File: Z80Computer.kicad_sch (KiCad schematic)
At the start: 4 parts, among them U1 Z80CPU, U2 28C256, X1 CXO_DIP14

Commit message: added more components
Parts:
- added DIS1: HD44780, 16026-16X2, symbol Z80ComputerLib:HD44780
- added R1: R_Small, symbol Z80ComputerLib:R_Small
- added RV1: R_Potentiometer, symbol Device:R_Potentiometer
- added SW1: SW_Push, symbol Z80ComputerLib:SW_Push
- added U4: 74LS138, symbol Z80ComputerLib:74LS138
- added U5: 74LS00, symbol Z80ComputerLib:74LS00
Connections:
- net +5V: now also U1.16 (~{INT}), U1.17 (~{NMI}), U1.24 (~{WAIT}), U1.25 (~{BUSRQ}), U2.27 (~{WE}), DIS1.P$15, DIS1.P$2, R1.1, RV1.1, U4.16 (VCC)
- net A0: now also DIS1.P$4
- net A4: now also U4.4 (E1)
- net A5: now also U4.1 (A0)
- net A6: now also U4.2 (A1)
- net A7: now also U4.3 (A2)
- net D0: now also DIS1.P$7
- net D1: now also DIS1.P$8
- net D2: now also DIS1.P$9
- net D3: now also DIS1.P$10
- net D4: now also DIS1.P$11
- net D5: now also DIS1.P$12
- net D6: now also DIS1.P$13
- net D7: now also DIS1.P$14
- net GND: now also DIS1.P$1, DIS1.P$16, RV1.3, SW1.1, U4.8 (GND)
- net ~{RD}: now also U5.1, U5.2
- net ~{IORQ}: now reaches U1.20 (~{IORQ})
- net ~{IORQ}: now also U4.5 (E2)
- net at U1.26 (~{RESET}): now also R1.2, SW1.2
- net ~{M1}: now reaches U1.27 (~{M1})
- net ~{M1}: now also U4.6 (E3)
- new net: U4.15 (O0), U5.4, U5.5
- new net: DIS1.P$3, RV1.2
- new net: DIS1.P$5, U5.3
- new net: DIS1.P$6, U5.6
- no-connect marks 0 -> 13
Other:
- moved on the sheet: X1

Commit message: got most of the circuit done apart from key pad
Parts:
- removed U3: ~, symbol Z80ComputerLib:YouTube
- added J1: Conn_Coaxial_Power, Connector_Coaxial:SMA_Amphenol_901-143_Horizontal, symbol Connector:Conn_Coaxial_Power
- added unit 5 of U5
- added unit 4 of U5
- added unit 3 of U5
- added U6: KM62256CLP, Package_DIP:DIP-28_W15.24mm, symbol Z80ComputerLib:KM62256CLP
- added U7: 74LS00, Package_DIP:DIP-14_W7.62mm, symbol Z80ComputerLib:74LS00
- DIS1: footprint 16026-16X2 -> Downloads:16026-16X2
- R1: footprint (none) -> Resistor_THT:R_Axial_DIN0204_L3.6mm_D1.6mm_P1.90mm_Vertical
- RV1: footprint (none) -> Potentiometer_THT:Potentiometer_ACP_CA6-H2,5_Horizontal
- SW1: footprint (none) -> Button_Switch_THT:KSA_Tactile_SPST
- U1: footprint (none) -> Package_DIP:DIP-40_W25.4mm
- U2: footprint (none) -> Package_DIP:DIP-28_W15.24mm
- U4: footprint (none) -> Package_DIP:DIP-16_W7.62mm
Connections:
- net +5V: now also J1.1 (In), U5.14 (VCC), U6.28 (VCC), U7.14 (VCC)
- net A0: now also U6.10 (A0)
- net A1: now also U6.9 (A1)
- net A10: now also U6.21 (A10)
- net A11: now also U6.23 (A11)
- net A12: now also U6.2 (A12)
- net A13: now also U6.26 (A13)
- net A14: now also U6.1 (A14)
- net A15: now also U7.1, U7.4, U7.5
- net A2: now also U6.8 (A2)
- net A3: now also U6.7 (A3)
- net A4: now also U6.6 (A4)
- net A5: now also U6.5 (A5)
- net A6: now also U6.4 (A6)
- net A7: now also U6.3 (A7)
- net A8: now also U6.25 (A8)
- net A9: now also U6.24 (A9)
- net D0: now also U6.11 (Q0)
- net D1: now also U6.12 (Q1)
- net D2: now also U6.13 (Q2)
- net D3: now also U6.15 (Q3)
- net D4: now also U6.16 (Q4)
- net D5: now also U6.17 (Q5)
- net D6: now also U6.18 (Q6)
- net D7: now also U6.19 (Q7)
- net GND: now also J1.2 (Ext), U5.7 (GND), U6.14 (GND), U7.7 (GND)
- net ~{MREQ}: now also U5.10, U7.2; no longer U2.20 (~{CS})
- net ~{RD}: now also U6.22 (~{OE})
- net ~{WR}: now reaches U1.22 (~{WR})
- net ~{WR}: now also U6.27 (~{WE})
- new net: U2.20 (~{CS}), U7.3
- new net: U5.8, U6.20 (~{CS})
- new net: U5.9, U7.6
- no-connect marks 13 -> 20

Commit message: before auto route pcb
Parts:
- added C1, C2: 0.1uF, Capacitor_THT:CP_Radial_D4.0mm_P1.50mm, symbol Z80ComputerLib:C
- added D1, D2, D3, D4, D5, D6, D7, D8: 1N4148, Diode_THT:D_DO-35_SOD27_P7.62mm_Horizontal, symbol Diode:1N4148
- added D9: LED, LED_THT:LED_D5.0mm, symbol Device:LED
- added J2, J3: Conn_01x08_Pin, Connector_JST:JST_EH_B8B-EH-A_1x08_P2.50mm_Vertical, symbol Connector:Conn_01x08_Pin
- added R10: 440R, Resistor_THT:R_Axial_DIN0204_L3.6mm_D1.6mm_P1.90mm_Vertical, symbol Z80ComputerLib:R_Small
- added R2, R3, R4, R5, R6, R7, R8, R9: 10K, Resistor_THT:R_Axial_DIN0204_L3.6mm_D1.6mm_P1.90mm_Vertical, symbol Z80ComputerLib:R_Small
- added U1: 74LS244, Package_DIP:DIP-20_W7.62mm, symbol Z80ComputerLib:74LS244
- added U2: 74LS32, Package_DIP:DIP-14_W7.62mm, symbol 74xx:74LS32
- added U3: 74LS273, Package_DIP:DIP-20_W7.62mm, symbol Z80ComputerLib:74LS273
- R1: value R_Small -> 1K
- U5, U7: footprint (none) -> Package_DIP:DIP-14_W7.62mm
- renumbered U1 to IC1, U2 to IC2_EEPROM1, U6 to IC6_SRAM1
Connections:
- net +5V: now also C1.1, C2.2, D9.1 (K), U1.20 (VCC), U2.14 (VCC), U3.1 (~{Mr}), U3.20 (VCC)
- net D0: now also U1.2 (I0a), U3.3 (D0)
- net D1: now also U1.4 (I1a), U3.4 (D1)
- net D2: now also U1.6 (I2a), U3.7 (D2)
- net D3: now also U1.8 (I3a), U3.8 (D3)
- net D4: now also U1.11 (I0b), U3.13 (D4)
- net D5: now also U1.13 (I1b), U3.14 (D5)
- net D6: now also U1.15 (I2b), U3.17 (D6)
- net D7: now also U1.17 (I3b), U3.18 (D7)
- net GND: now also C1.2, C2.1, R10.2, R2.2, R3.2, R4.2, R5.2, R6.2, R7.2, R8.2, R9.2, U1.10 (GND), U2.7 (GND), U3.10 (GND)
- net ~{RD}: now also U2.2
- net ~{WR}: now also U2.4
- net ~{KEYPAD_PORT}: now reaches U4.14 (O1)
- net ~{KEYPAD_PORT}: now also U2.1, U2.5
- net ~{LCD_OUT_PORT}: now reaches U4.15 (O0), U5.4, U5.5
- new net: J2.3 (Pin_3), R7.1, U1.14 (O2a)
- new net: J2.2 (Pin_2), R8.1, U1.16 (O1a)
- new net: J2.5 (Pin_5), R5.1, U1.9 (O0b)
- new net: D1.1 (K), J3.1 (Pin_1)
- new net: D8.1 (K), J3.2 (Pin_2)
- new net: D3.1 (K), J3.3 (Pin_3)
- new net: D2.1 (K), J3.4 (Pin_4)
- new net: D4.1 (K), J3.5 (Pin_5)
- new net: D6.1 (K), J3.6 (Pin_6)
- new net: D5.1 (K), J3.7 (Pin_7)
- new net: D7.1 (K), J3.8 (Pin_8)
- new net: D7.2 (A), U3.19 (Q7)
- new net: D6.2 (A), U3.15 (Q5)
- new net: D9.2 (A), R10.1
- new net: D1.2 (A), U3.2 (Q0)
- new net: D5.2 (A), U3.16 (Q6)
- new net: J2.8 (Pin_8), R2.1, U1.3 (O3b)
- new net: D8.2 (A), U3.5 (Q1)
- new net: J2.7 (Pin_7), R4.1, U1.5 (O2b)
- new net: U2.6, U3.11 (Cp)
- new net: D4.2 (A), U3.12 (Q4)
- new net: D3.2 (A), U3.6 (Q2)
- new net: D2.2 (A), U3.9 (Q3)
- new net: J2.1 (Pin_1), R9.1, U1.18 (O0a)
- new net: J2.4 (Pin_4), R6.1, U1.12 (O3a)
- new net: U1.1 (OEa), U1.19 (OEb), U2.3
- new net: J2.6 (Pin_6), R3.1, U1.7 (O1b)
- no-connect marks 20 -> 25
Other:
- title: (none) -> Minimal Z80 Computer
- moved on the sheet: DIS1, J1, U5A, U5B, U5C, U5D, U5E, U7B, U7C, U7D, U7E

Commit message: reworked to correct z80 footprint
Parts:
- IC1: footprint Package_DIP:DIP-40_W25.4mm -> Package_DIP:DIP-40_W15.24mm
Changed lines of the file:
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@@
       (effects (font (size 1.27 1.27)) (justify left))
     )
-    (property "Footprint" "Package_DIP:DIP-40_W25.4mm" (at 109.22 86.36 0)
+    (property "Footprint" "Package_DIP:DIP-40_W15.24mm" (at 109.22 86.36 0)
       (effects (font (size 1.27 1.27)) hide)
     )

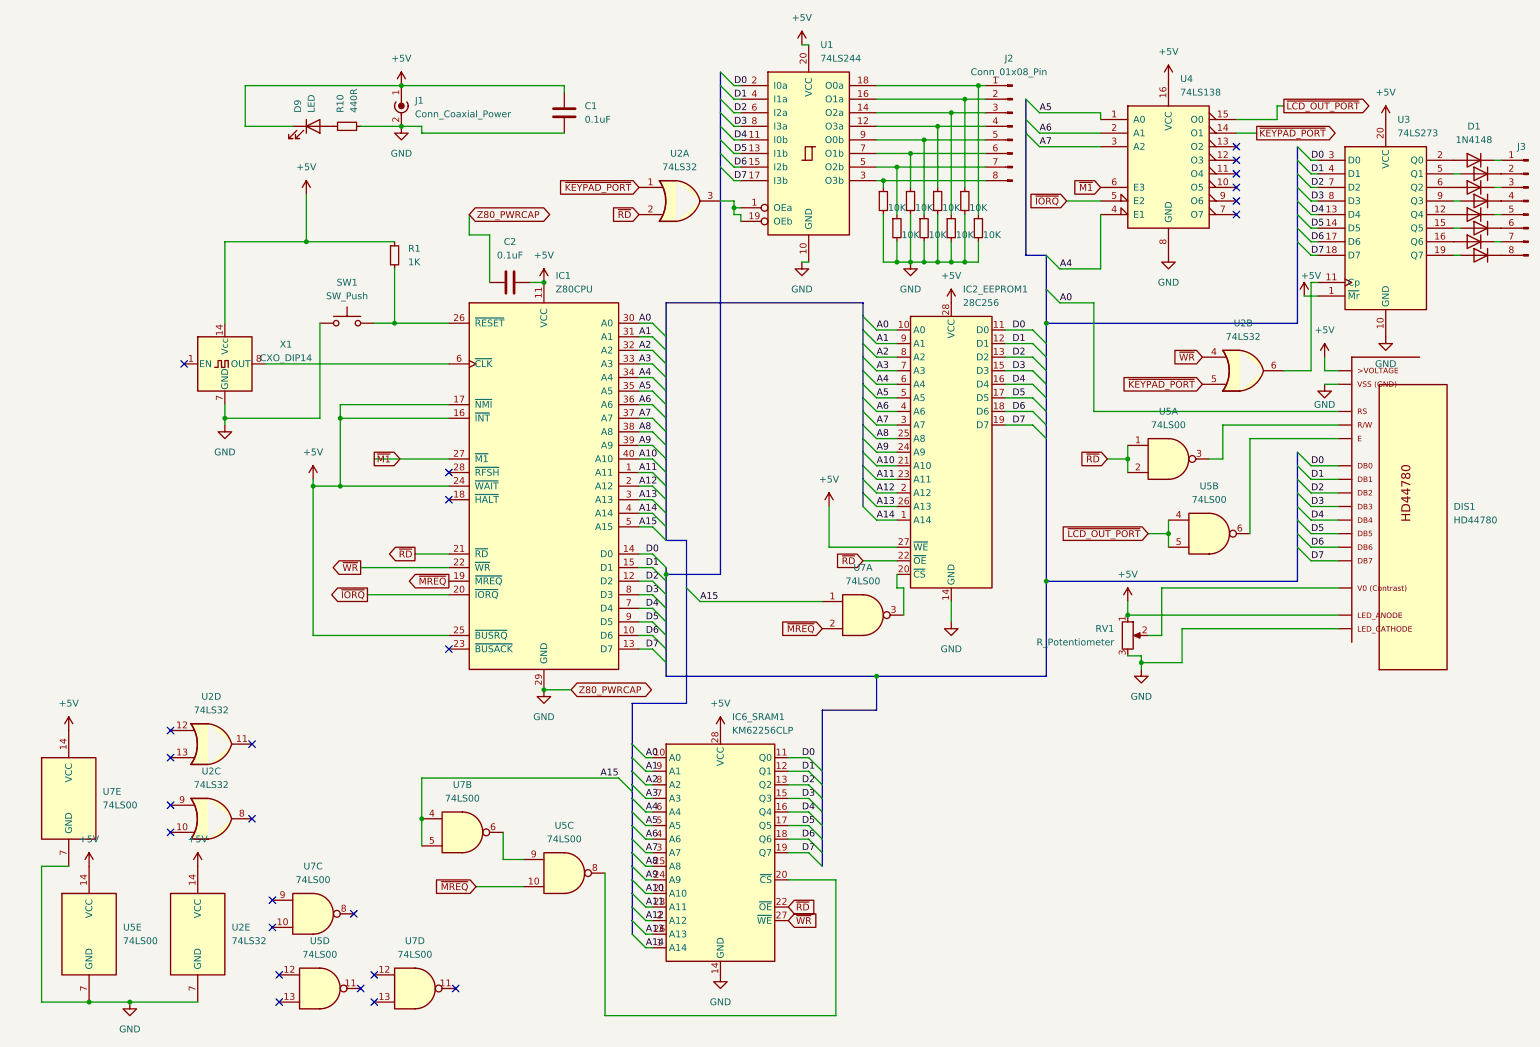
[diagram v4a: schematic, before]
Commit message: Added RC reset and fixed RAM ROM chip select
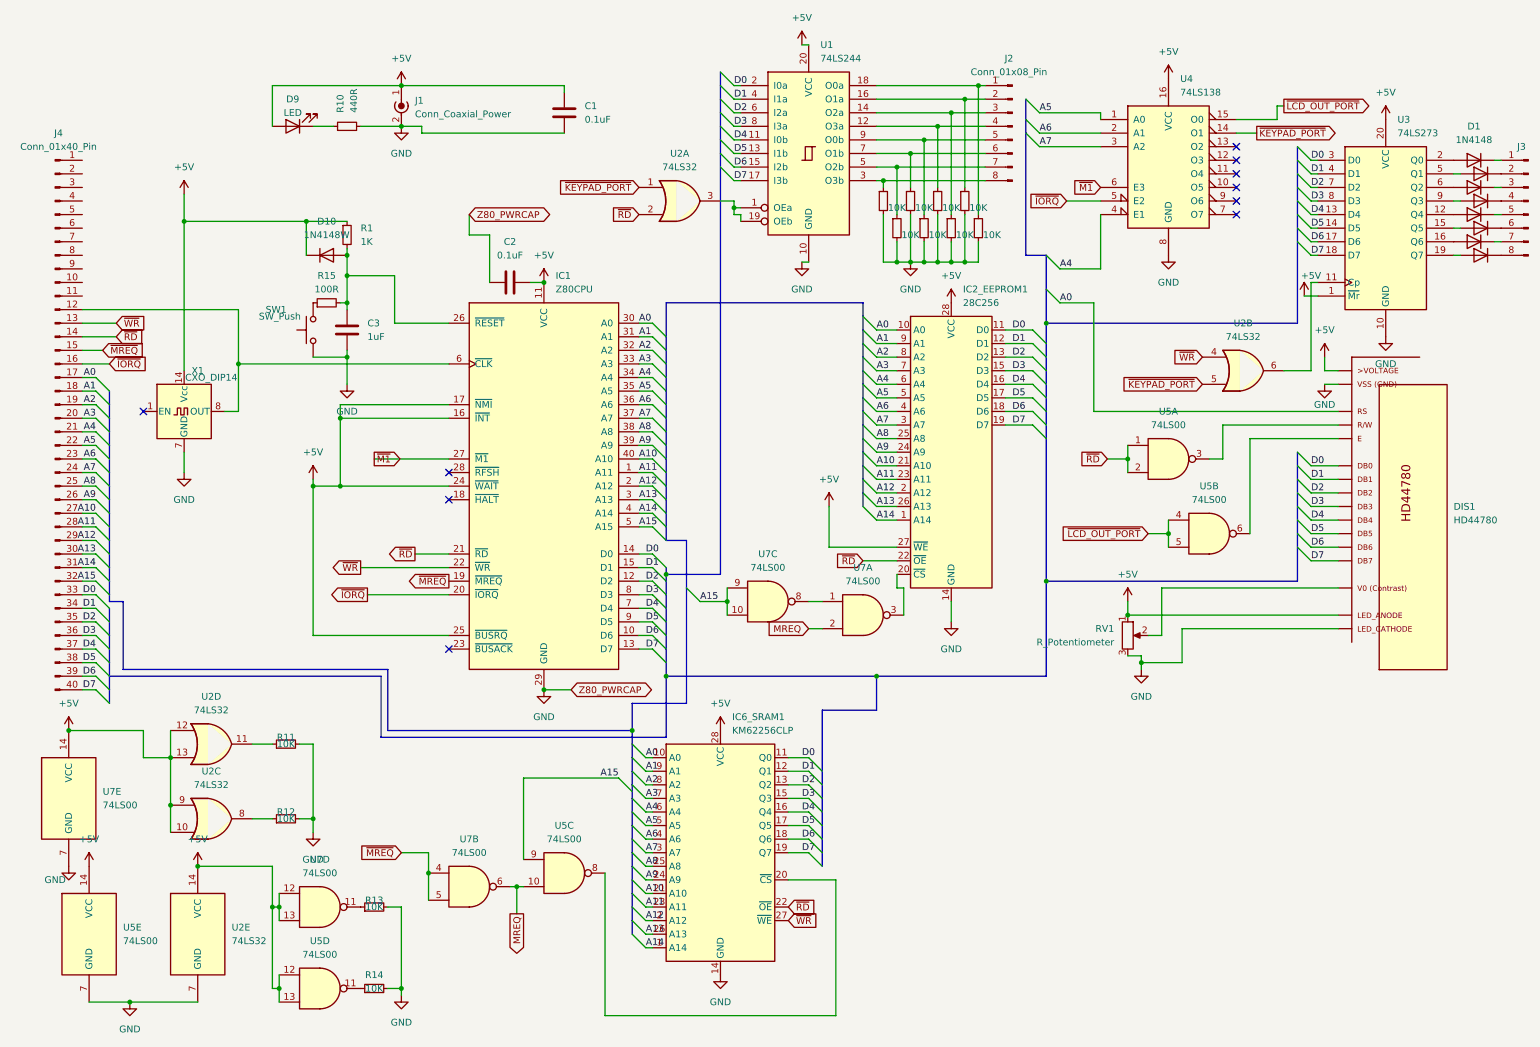
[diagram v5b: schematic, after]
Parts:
- added C3: 1uF, symbol Z80ComputerLib:C
- added D10: 1N4148W, Diode_SMD:D_SOD-123, symbol Diode:1N4148W
- added J4: Conn_01x40_Pin, symbol Connector:Conn_01x40_Pin
- added R11, R12, R13, R14: 10K, Resistor_THT:R_Axial_DIN0204_L3.6mm_D1.6mm_P1.90mm_Vertical, symbol Z80ComputerLib:R_Small
- added R15: 100R, symbol Z80ComputerLib:R_Small
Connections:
- net +5V: now also D9.2 (A), U2.10, U2.12, U2.13, U2.9, U5.12, U5.13, U7.12, U7.13, D10.1 (K); no longer D9.1 (K)
- net A0: now also J4.17 (Pin_17)
- net A1: now also J4.18 (Pin_18)
- net A10: now also J4.27 (Pin_27)
- net A11: now also J4.28 (Pin_28)
- net A12: now also J4.29 (Pin_29)
- net A13: now also J4.30 (Pin_30)
- net A14: now also J4.31 (Pin_31)
- net A15: now also U5.9, U7.10, U7.9, J4.32 (Pin_32); no longer U7.1, U7.4, U7.5
- net A2: now also J4.19 (Pin_19)
- net A3: now also J4.20 (Pin_20)
- net A4: now also J4.21 (Pin_21)
- net A5: now also J4.22 (Pin_22)
- net A6: now also J4.23 (Pin_23)
- net A7: now also J4.24 (Pin_24)
- net A8: now also J4.25 (Pin_25)
- net A9: now also J4.26 (Pin_26)
- net D0: now also J4.33 (Pin_33)
- net D1: now also J4.34 (Pin_34)
- net D2: now also J4.35 (Pin_35)
- net D3: now also J4.36 (Pin_36)
- net D4: now also J4.37 (Pin_37)
- net D5: now also J4.38 (Pin_38)
- net D6: now also J4.39 (Pin_39)
- net D7: now also J4.40 (Pin_40)
- net GND: now also C3.2, R11.2, R12.2, R13.2, R14.2
- net ~{IORQ}: now also J4.16 (Pin_16)
- net ~{MREQ}: now also U7.4, U7.5, J4.15 (Pin_15); no longer U5.10, U7.2
- net ~{RD}: now also J4.14 (Pin_14)
- net ~{WR}: now also J4.13 (Pin_13)
- net at U2.11: now also R11.1
- net at IC1.26 (~{RESET}), R1.2: now also C3.1, D10.2 (A), R15.2; no longer SW1.2
- net at R10.1: now also D9.1 (K); no longer D9.2 (A)
- net at IC1.6 (~{CLK}), X1.8 (OUT): now also J4.12 (Pin_12)
- net at U2.8: now also R12.1
- net at U7.11: now also R13.1
- net at U7.8: now also U7.1
- net at U5.11: now also R14.1
- net MREQ: now reaches U7.6
- net MREQ: now also U5.10, U7.2; no longer U5.9
- new net: R15.1, SW1.2
- no-connect marks 25 -> 10
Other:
- moved on the sheet: D9, R1, SW1, U7B, U7C, U7D, X1

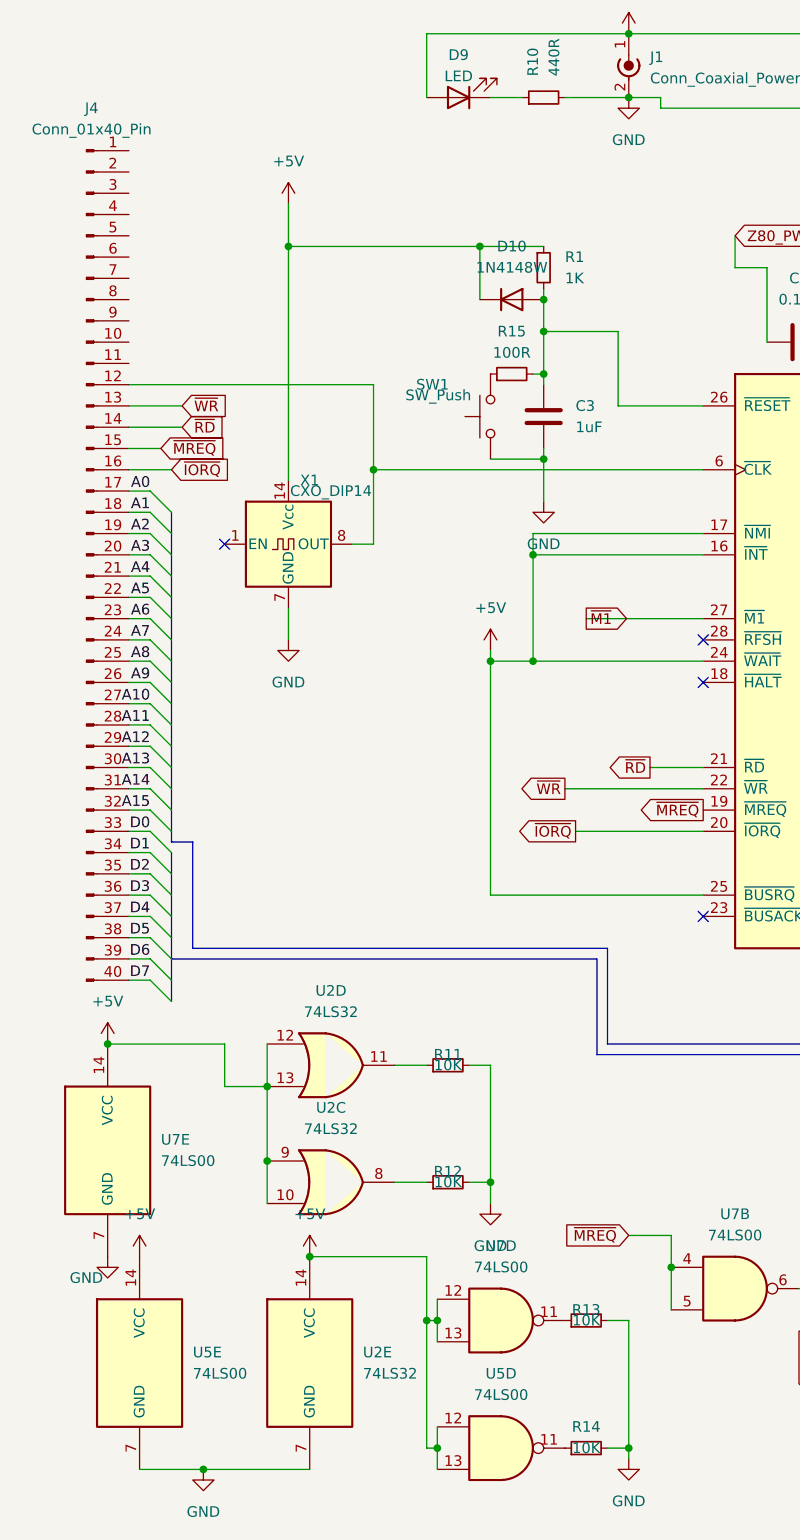
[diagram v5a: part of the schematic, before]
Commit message: added some footprints and updated pcb
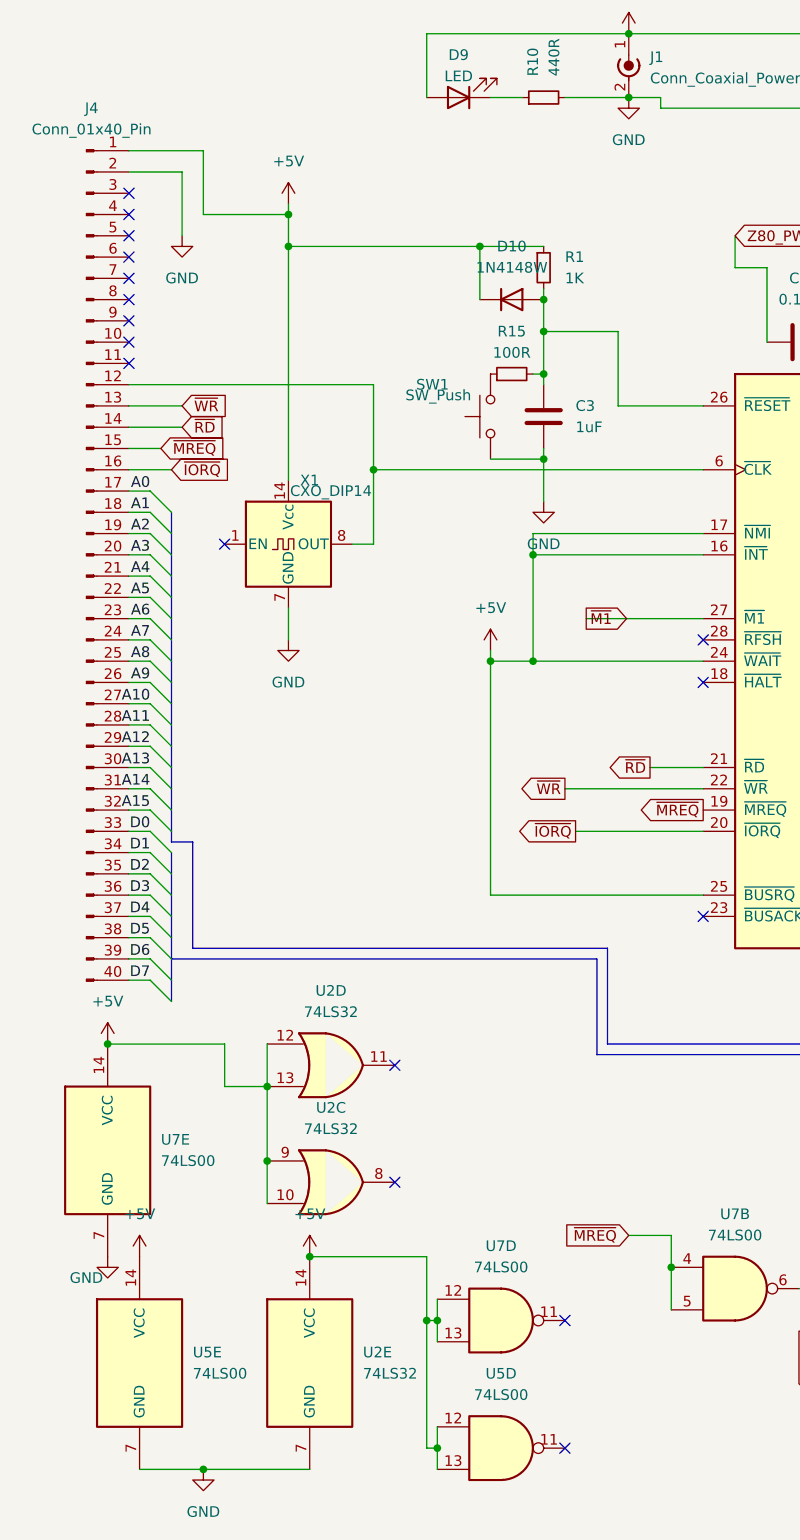
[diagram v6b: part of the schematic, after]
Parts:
- removed R11, R12, R13, R14: 10K, Resistor_THT:R_Axial_DIN0204_L3.6mm_D1.6mm_P1.90mm_Vertical, symbol Z80ComputerLib:R_Small
- C3: footprint (none) -> Capacitor_THT:CP_Axial_L10.0mm_D4.5mm_P15.00mm_Horizontal
- J4: footprint (none) -> Connector_PCBEdge:Samtec_MECF-40-0_-NP-L-DV_2x40_P1.27mm_Edge
- R15: footprint (none) -> Resistor_THT:R_Axial_DIN0204_L3.6mm_D1.6mm_P1.90mm_Vertical
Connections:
- net +5V: now also J4.1 (Pin_1)
- net GND: now also J4.2 (Pin_2)
- no-connect marks 10 -> 23
